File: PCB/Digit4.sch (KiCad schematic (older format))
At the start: 1 part

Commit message: Worked on PCB.
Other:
- moved on the sheet: D3D
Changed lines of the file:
@@
 L LED_Array D3
 U 4 1 54BC7685
-P 4800 4150
-F 0 "D3" H 4800 5300 50  0000 C CNN
-F 1 "LED_Array" H 4800 5400 50  0000 C CNN
-F 2 "Custom:LED-ARRAY" H 4800 5075 50  0001 C CNN
-F 3 "" H 4800 5075 50  0000 C CNN
-	4    4800 4150
+P 3750 4150
+F 0 "D3" H 3750 5300 50  0000 C CNN
+F 1 "LED_Array" H 3750 5400 50  0000 C CNN
+F 2 "Custom:LED-ARRAY" H 3750 5075 50  0001 C CNN
+F 3 "" H 3750 5075 50  0000 C CNN
+	4    3750 4150
 	1    0    0    -1
 $EndComp

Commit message: Updated schematic.
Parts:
- added Q? (x14): FDG1024NZ, SC70-6, symbol FDG1024NZ
- added R? (x14): 10K, symbol R
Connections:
- net labels added: D1A1, D1A2, D1A3, D1A4, D1A5, D1A6, D1S1G, D1S1R, D1S2G, D1S2R, D1S3G, D1S3R, D1S4G, D1S4R, D1S5G, D1S5R, D1S6G, D1S6R, D1S7G, D1S7R, GND
- wire segments 0 -> 257
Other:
- moved on the sheet: D3D

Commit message: Updated schematic.
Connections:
- net labels added: D4A1, D4A2, D4A3, D4A4, D4A5, D4A6, D4S1G, D4S1R, D4S2G, D4S2R, D4S3G, D4S3R, D4S4G, D4S4R, D4S5G, D4S5R, D4S6G, D4S6R, D4S7G, D4S7R
- net labels removed: D1A1, D1A2, D1A3, D1A4, D1A5, D1A6, D1S1G, D1S1R, D1S2G, D1S2R, D1S3G, D1S3R, D1S4G, D1S4R, D1S5G, D1S5R, D1S6G, D1S6R, D1S7G, D1S7R
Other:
- moved on the sheet: D3D, R?

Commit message: Updated mosfets.
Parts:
- removed Q? (x14): FDG1024NZ, SC70-6, symbol FDG1024NZ
- added Q? (x14): DMN2041LSD-13, SO-8, symbol DMN2041LSD-13
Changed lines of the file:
@@
 D4A6
-$Comp
-L FDG1024NZ Q?
-U 1 1 54EADD7E
-P 1350 2350
-F 0 "Q?" H 1350 2201 40  0000 R CNN
-F 1 "FDG1024NZ" H 1350 2500 40  0000 R CNN
-F 2 "SC70-6" H 1220 2452 29  0000 C CNN
-F 3 "" H 1350 2350 60  0000 C CNN
-	1    1350 2350
-	1    0    0    -1
-$EndComp
-$Comp
-L FDG1024NZ Q?
-U 1 1 54EADD85
-P 2350 2350
-F 0 "Q?" H 2350 2201 40  0000 R CNN
-F 1 "FDG1024NZ" H 2350 2500 40  0000 R CNN
-F 2 "SC70-6" H 2220 2452 29  0000 C CNN
-F 3 "" H 2350 2350 60  0000 C CNN
-	1    2350 2350
-	1    0    0    -1
-$EndComp
 $Comp
 L R R?
@@
 $EndComp
 $Comp
-L FDG1024NZ Q?
-U 1 1 54EADDA6
-P 1350 5050
-F 0 "Q?" H 1350 4901 40  0000 R CNN
-F 1 "FDG1024NZ" H 1350 5200 40  0000 R CNN
-F 2 "SC70-6" H 1220 5152 29  0000 C CNN
-F 3 "" H 1350 5050 60  0000 C CNN
-	1    1350 5050
-	1    0    0    -1
-$EndComp
-$Comp
 L R R?
 U 1 1 54EADDAD
@@
 D4S5G
 $Comp
-L FDG1024NZ Q?
-U 1 1 54EADDCB
-P 2350 5050
-F 0 "Q?" H 2350 4901 40  0000 R CNN
-F 1 "FDG1024NZ" H 2350 5200 40  0000 R CNN
-F 2 "SC70-6" H 2220 5152 29  0000 C CNN
-F 3 "" H 2350 5050 60  0000 C CNN
-	1    2350 5050
-	1    0    0    -1
-$EndComp
-$Comp
-L FDG1024NZ Q?
-U 1 1 54EADDD2
-P 1350 6825
-F 0 "Q?" H 1350 6676 40  0000 R CNN
-F 1 "FDG1024NZ" H 1350 6975 40  0000 R CNN
-F 2 "SC70-6" H 1220 6927 29  0000 C CNN
-F 3 "" H 1350 6825 60  0000 C CNN
-	1    1350 6825
-	1    0    0    -1
-$EndComp
-$Comp
 L R R?
 U 1 1 54EADDD9
@@
 Text HLabel 1900 6875 0    50   Input ~ 0
 D4S4G
-$Comp
-L FDG1024NZ Q?
-U 1 1 54EADDF5
-P 2350 6825
-F 0 "Q?" H 2350 6676 40  0000 R CNN
-F 1 "FDG1024NZ" H 2350 6975 40  0000 R CNN
-F 2 "SC70-6" H 2220 6927 29  0000 C CNN
-F 3 "" H 2350 6825 60  0000 C CNN
-	1    2350 6825
-	1    0    0    -1
-$EndComp
 Wire Wire Line
 	3705 1150 3705 950
@@
 Wire Wire Line
 	2450 6625 2450 6500
-$Comp
-L FDG1024NZ Q?
-U 1 1 54EADF15
-P 7700 1125
-F 0 "Q?" H 7700 976 40  0000 R CNN
-F 1 "FDG1024NZ" H 7700 1275 40  0000 R CNN
-F 2 "SC70-6" H 7570 1227 29  0000 C CNN
-F 3 "" H 7700 1125 60  0000 C CNN
-	1    7700 1125
-	1    0    0    -1
-$EndComp
 $Comp
 L R R?
@@
 Text HLabel 8250 1175 0    50   Input ~ 0
 D4S1G
-$Comp
-L FDG1024NZ Q?
-U 1 1 54EADF38
-P 8700 1125
-F 0 "Q?" H 8700 976 40  0000 R CNN
-F 1 "FDG1024NZ" H 8700 1275 40  0000 R CNN
-F 2 "SC70-6" H 8570 1227 29  0000 C CNN
-F 3 "" H 8700 1125 60  0000 C CNN
-	1    8700 1125
-	1    0    0    -1
-$EndComp
 Wire Wire Line
 	8250 1175 8500 1175
@@
 Wire Wire Line
 	8800 675  8800 925
-$Comp
-L FDG1024NZ Q?
-U 1 1 54EADF4E
-P 7700 2625
-F 0 "Q?" H 7700 2476 40  0000 R CNN
-F 1 "FDG1024NZ" H 7700 2775 40  0000 R CNN
-F 2 "SC70-6" H 7570 2727 29  0000 C CNN
-F 3 "" H 7700 2625 60  0000 C CNN
-	1    7700 2625
-	1    0    0    -1
-$EndComp
 $Comp
 L R R?
@@
 Text HLabel 8250 2675 0    50   Input ~ 0
 D4S2G
-$Comp
-L FDG1024NZ Q?
-U 1 1 54EADF71
-P 8700 2625
-F 0 "Q?" H 8700 2476 40  0000 R CNN
-F 1 "FDG1024NZ" H 8700 2775 40  0000 R CNN
-F 2 "SC70-6" H 8570 2727 29  0000 C CNN
-F 3 "" H 8700 2625 60  0000 C CNN
-	1    8700 2625
-	1    0    0    -1
-$EndComp
 Wire Wire Line
 	8250 2675 8500 2675
@@
 Wire Wire Line
 	8800 2125 8800 2425
-$Comp
-L FDG1024NZ Q?
-U 1 1 54EADF88
-P 7700 5485
-F 0 "Q?" H 7700 5336 40  0000 R CNN
-F 1 "FDG1024NZ" H 7700 5635 40  0000 R CNN
-F 2 "SC70-6" H 7570 5587 29  0000 C CNN
-F 3 "" H 7700 5485 60  0000 C CNN
-	1    7700 5485
-	1    0    0    -1
-$EndComp
 $Comp
 L R R?
@@
 Text HLabel 8250 5535 0    50   Input ~ 0
 D4S3G
-$Comp
-L FDG1024NZ Q?
-U 1 1 54EADFAB
-P 8700 5485
-F 0 "Q?" H 8700 5336 40  0000 R CNN
-F 1 "FDG1024NZ" H 8700 5635 40  0000 R CNN
-F 2 "SC70-6" H 8570 5587 29  0000 C CNN
-F 3 "" H 8700 5485 60  0000 C CNN
-	1    8700 5485
-	1    0    0    -1
-$EndComp
 Wire Wire Line
 	8250 5535 8500 5535
@@
 Wire Wire Line
 	7800 750  7800 925
-$Comp
-L FDG1024NZ Q?
-U 1 1 54EADFC3
-P 7700 4010
-F 0 "Q?" H 7700 3861 40  0000 R CNN
-F 1 "FDG1024NZ" H 7700 4160 40  0000 R CNN
-F 2 "SC70-6" H 7570 4112 29  0000 C CNN
-F 3 "" H 7700 4010 60  0000 C CNN
-	1    7700 4010
-	1    0    0    -1
-$EndComp
 $Comp
 L R R?
@@
 Text HLabel 8250 4060 0    50   Input ~ 0
 D4S7G
-$Comp
-L FDG1024NZ Q?
-U 1 1 54EADFE6
-P 8700 4010
-F 0 "Q?" H 8700 3861 40  0000 R CNN
-F 1 "FDG1024NZ" H 8700 4160 40  0000 R CNN
-F 2 "SC70-6" H 8570 4112 29  0000 C CNN
-F 3 "" H 8700 4010 60  0000 C CNN
-	1    8700 4010
-	1    0    0    -1
-$EndComp
 Wire Wire Line
 	8250 4060 8500 4060
@@
 EndData
 $EndBitmap
+$Comp
+L DMN2041LSD-13 Q?
+U 1 1 54ED5347
+P 1350 2350
+F 0 "Q?" H 1350 2201 40  0000 R CNN
+F 1 "DMN2041LSD-13" H 1350 2500 40  0000 R CNN
+F 2 "SO-8" H 1220 2452 29  0001 C CNN
+F 3 "" H 1350 2350 60  0000 C CNN
+	1    1350 2350
+	1    0    0    -1
+$EndComp
+$Comp
+L DMN2041LSD-13 Q?
+U 2 1 54ED5384
+P 2350 2350
+F 0 "Q?" H 2350 2201 40  0000 R CNN
+F 1 "DMN2041LSD-13" H 2350 2500 40  0000 R CNN
+F 2 "SO-8" H 2220 2452 29  0001 C CNN
+F 3 "" H 2350 2350 60  0000 C CNN
+	2    2350 2350
+	1    0    0    -1
+$EndComp
+$Comp
+L DMN2041LSD-13 Q?
+U 1 1 54ED5743
+P 1350 5050
+F 0 "Q?" H 1350 4901 40  0000 R CNN
+F 1 "DMN2041LSD-13" H 1350 5200 40  0000 R CNN
+F 2 "SO-8" H 1220 5152 29  0001 C CNN
+F 3 "" H 1350 5050 60  0000 C CNN
+	1    1350 5050
+	1    0    0    -1
+$EndComp
+$Comp
+L DMN2041LSD-13 Q?
+U 2 1 54ED577C
+P 2350 5050
+F 0 "Q?" H 2350 4901 40  0000 R CNN
+F 1 "DMN2041LSD-13" H 2350 5200 40  0000 R CNN
+F 2 "SO-8" H 2220 5152 29  0001 C CNN
+F 3 "" H 2350 5050 60  0000 C CNN
+	2    2350 5050
+	1    0    0    -1
+$EndComp
+$Comp
+L DMN2041LSD-13 Q?
+U 1 1 54ED5997
+P 1350 6825
+F 0 "Q?" H 1350 6676 40  0000 R CNN
+F 1 "DMN2041LSD-13" H 1350 6975 40  0000 R CNN
+F 2 "SO-8" H 1220 6927 29  0001 C CNN
+F 3 "" H 1350 6825 60  0000 C CNN
+	1    1350 6825
+	1    0    0    -1
+$EndComp
+$Comp
+L DMN2041LSD-13 Q?
+U 2 1 54ED5AEE
+P 2350 6825
+F 0 "Q?" H 2350 6676 40  0000 R CNN
+F 1 "DMN2041LSD-13" H 2350 6975 40  0000 R CNN
+F 2 "SO-8" H 2220 6927 29  0001 C CNN
+F 3 "" H 2350 6825 60  0000 C CNN
+	2    2350 6825
+	1    0    0    -1
+$EndComp
+$Comp
+L DMN2041LSD-13 Q?
+U 1 1 54ED5CA8
+P 7700 5485
+F 0 "Q?" H 7700 5336 40  0000 R CNN
+F 1 "DMN2041LSD-13" H 7700 5635 40  0000 R CNN
+F 2 "SO-8" H 7570 5587 29  0001 C CNN
+F 3 "" H 7700 5485 60  0000 C CNN
+	1    7700 5485
+	1    0    0    -1
+$EndComp
+$Comp
+L DMN2041LSD-13 Q?
+U 2 1 54ED5D85
+P 8700 5485
+F 0 "Q?" H 8700 5336 40  0000 R CNN
+F 1 "DMN2041LSD-13" H 8700 5635 40  0000 R CNN
+F 2 "SO-8" H 8570 5587 29  0001 C CNN
+F 3 "" H 8700 5485 60  0000 C CNN
+	2    8700 5485
+	1    0    0    -1
+$EndComp
+$Comp
+L DMN2041LSD-13 Q?
+U 1 1 54ED5ECB
+P 7700 4010
+F 0 "Q?" H 7700 3861 40  0000 R CNN
+F 1 "DMN2041LSD-13" H 7700 4160 40  0000 R CNN
+F 2 "SO-8" H 7570 4112 29  0001 C CNN
+F 3 "" H 7700 4010 60  0000 C CNN
+	1    7700 4010
+	1    0    0    -1
+$EndComp
+$Comp
+L DMN2041LSD-13 Q?
+U 2 1 54ED5F20
+P 8700 4010
+F 0 "Q?" H 8700 3861 40  0000 R CNN
+F 1 "DMN2041LSD-13" H 8700 4160 40  0000 R CNN
+F 2 "SO-8" H 8570 4112 29  0001 C CNN
+F 3 "" H 8700 4010 60  0000 C CNN
+	2    8700 4010
+	1    0    0    -1
+$EndComp
+$Comp
+L DMN2041LSD-13 Q?
+U 1 1 54ED6335
+P 7700 2625
+F 0 "Q?" H 7700 2476 40  0000 R CNN
+F 1 "DMN2041LSD-13" H 7700 2775 40  0000 R CNN
+F 2 "SO-8" H 7570 2727 29  0001 C CNN
+F 3 "" H 7700 2625 60  0000 C CNN
+	1    7700 2625
+	1    0    0    -1
+$EndComp
+$Comp
+L DMN2041LSD-13 Q?
+U 2 1 54ED63B0
+P 8700 2625
+F 0 "Q?" H 8700 2476 40  0000 R CNN
+F 1 "DMN2041LSD-13" H 8700 2775 40  0000 R CNN
+F 2 "SO-8" H 8570 2727 29  0001 C CNN
+F 3 "" H 8700 2625 60  0000 C CNN
+	2    8700 2625
+	1    0    0    -1
+$EndComp
+$Comp
+L DMN2041LSD-13 Q?
+U 1 1 54ED6543
+P 7700 1125
+F 0 "Q?" H 7700 976 40  0000 R CNN
+F 1 "DMN2041LSD-13" H 7700 1275 40  0000 R CNN
+F 2 "SO-8" H 7570 1227 29  0001 C CNN
+F 3 "" H 7700 1125 60  0000 C CNN
+	1    7700 1125
+	1    0    0    -1
+$EndComp
+$Comp
+L DMN2041LSD-13 Q?
+U 2 1 54ED65B8
+P 8700 1125
+F 0 "Q?" H 8700 976 40  0000 R CNN
+F 1 "DMN2041LSD-13" H 8700 1275 40  0000 R CNN
+F 2 "SO-8" H 8570 1227 29  0001 C CNN
+F 3 "" H 8700 1125 60  0000 C CNN
+	2    8700 1125
+	1    0    0    -1
+$EndComp
 $EndSCHEMATC

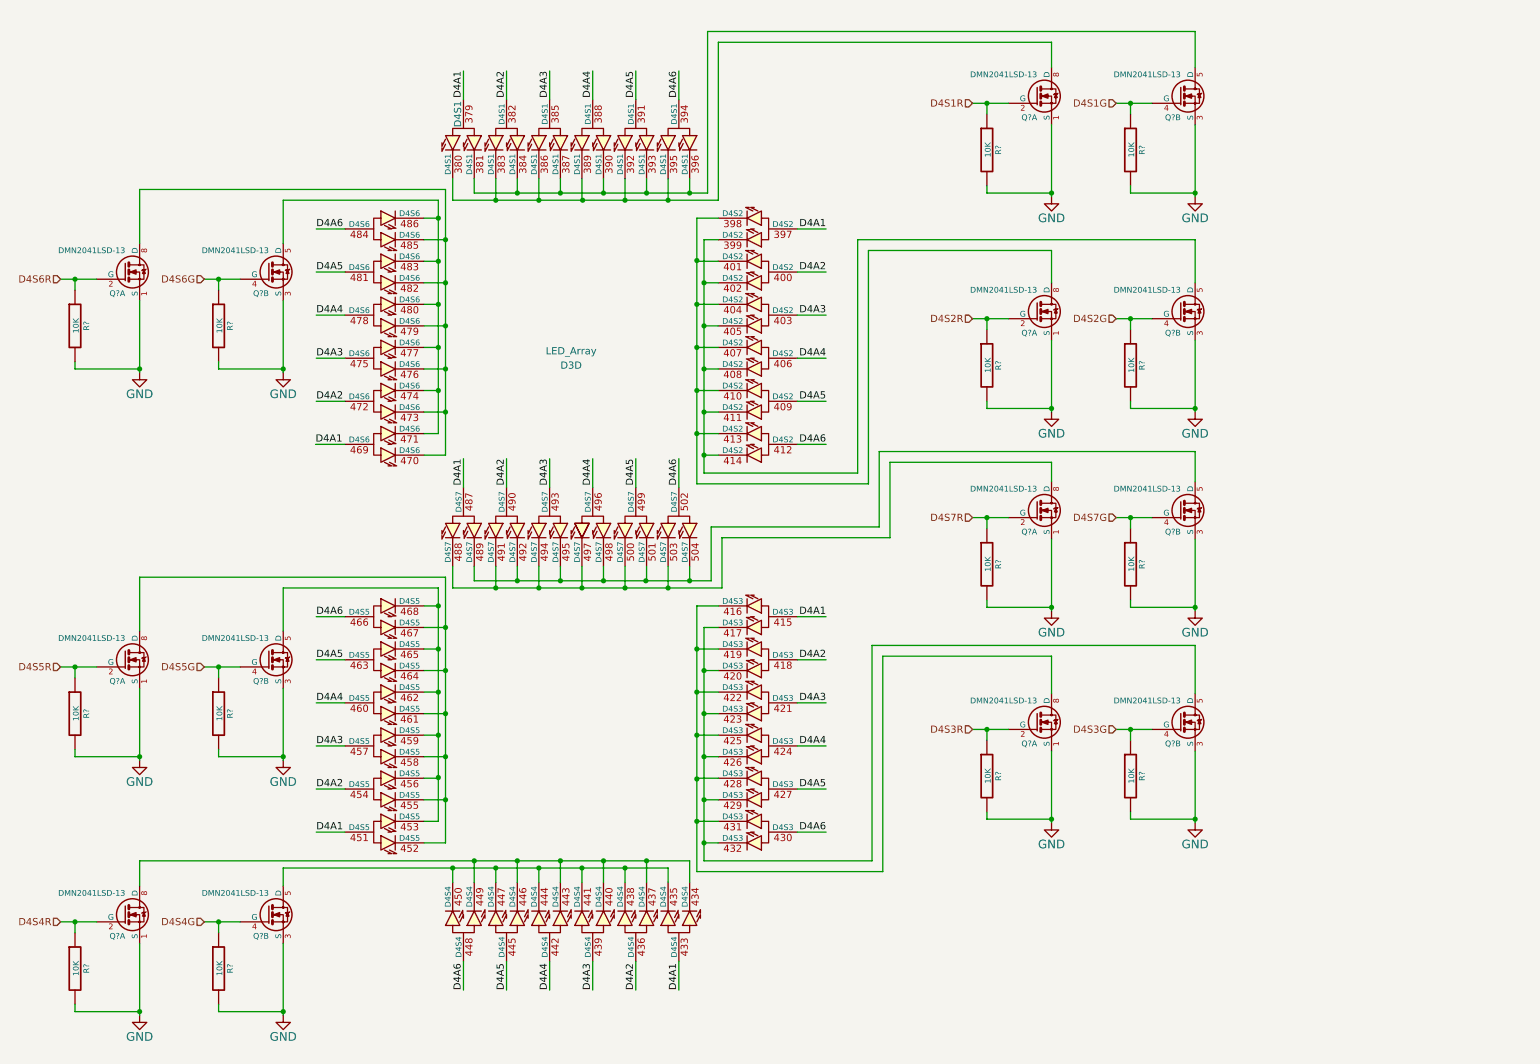
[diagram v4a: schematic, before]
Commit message: Added additional mosfets.
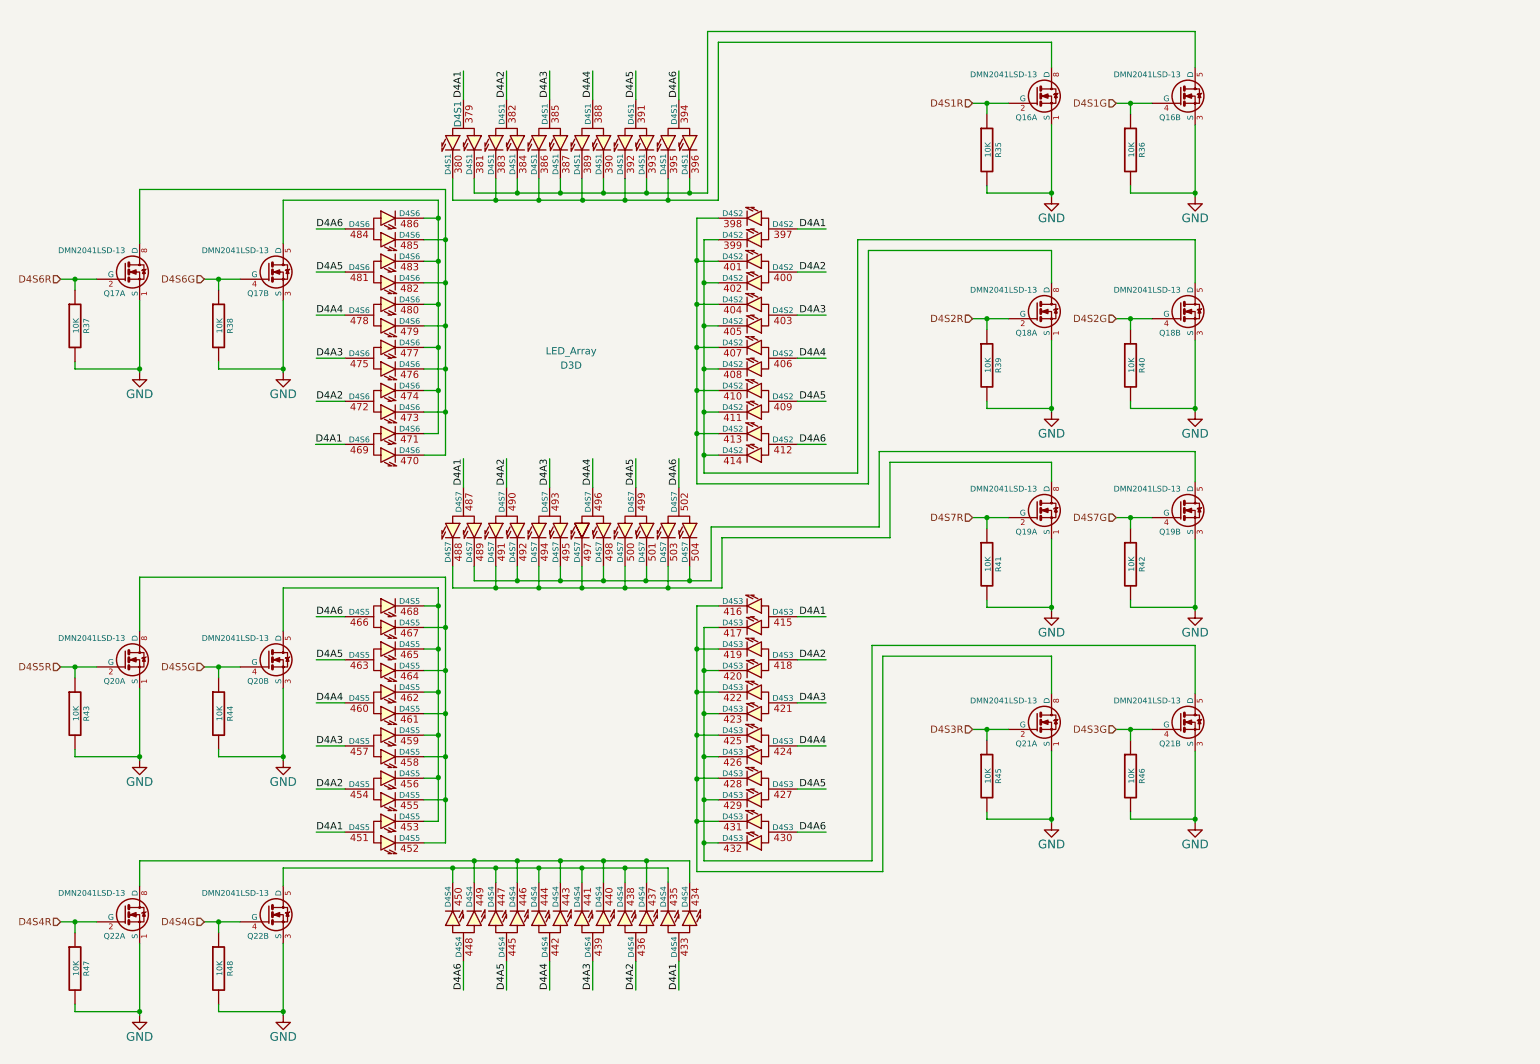
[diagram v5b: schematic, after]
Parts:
- Q16, Q17, Q18, Q19, Q20, Q21, Q22: renamed from Q?; footprint SO-8 -> Power_Integrations:SO-8
- R35, R36, R37, R38, R39, R40, R41, R42, R43, R44, R45, R46, R47, R48: renamed from R?; footprint (none) -> Resistors_SMD:R_0603_HandSoldering

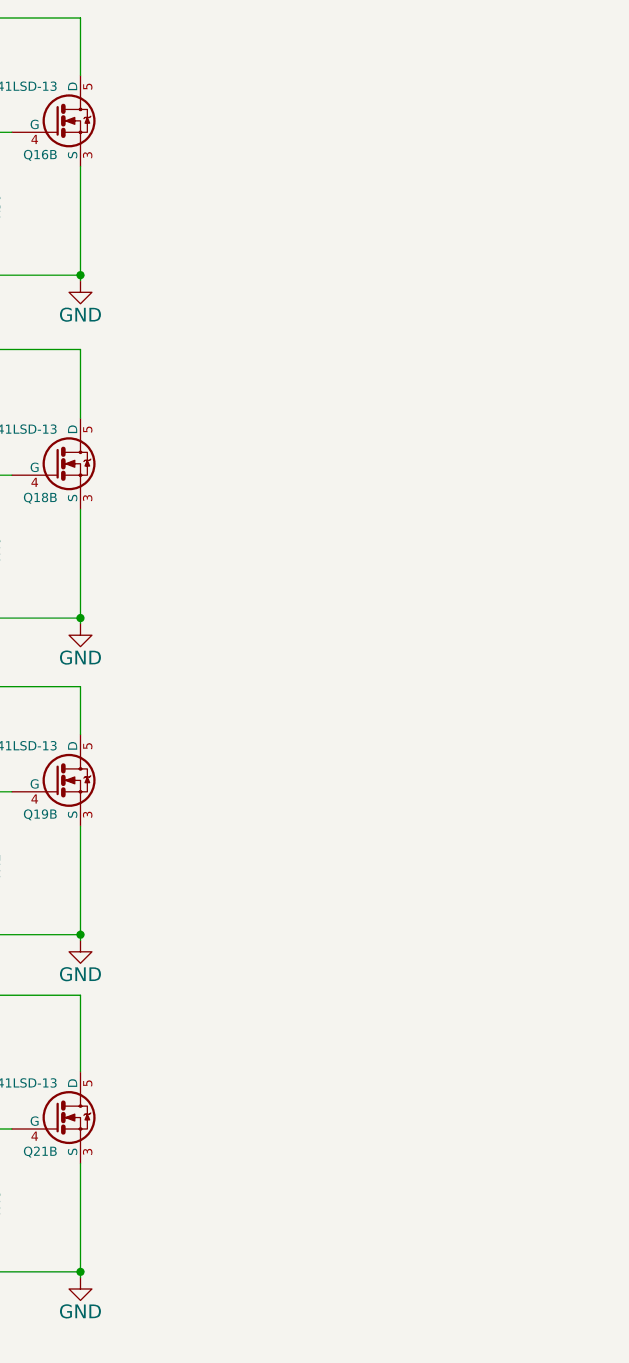
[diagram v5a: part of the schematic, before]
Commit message: Added additional mosfets.
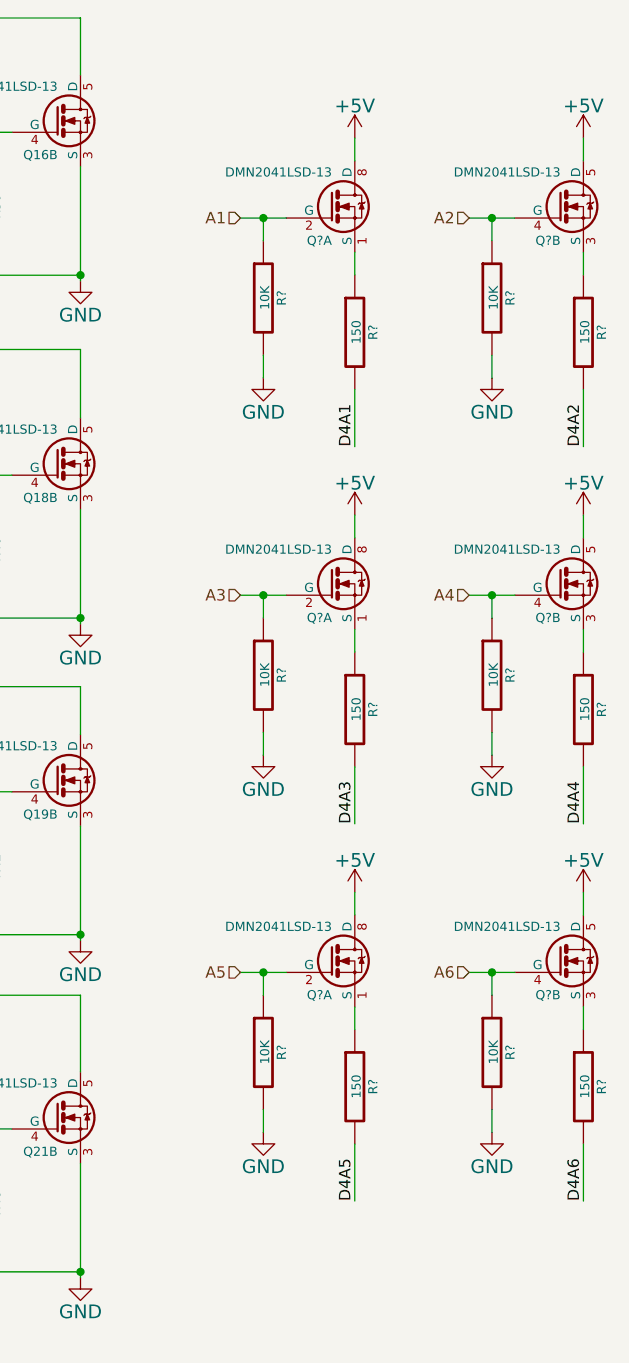
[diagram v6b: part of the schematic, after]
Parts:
- added Q? (x6): DMN2041LSD-13, SO-8, symbol DMN2041LSD-13
- added R? (x6): 10K, Resistors_SMD:R_0603_HandSoldering, symbol R
- added R? (x6): 150, Resistors_SMD:R_0603_HandSoldering, symbol R
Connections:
- net D4A1: now also R?.2
- net D4A2: now also R?.2
- net D4A3: now also R?.2
- net D4A4: now also R?.2
- net D4A5: now also R?.2
- net D4A6: now also R?.2
- net GND: now also R?.2, R?.2, R?.2, R?.2, R?.2, R?.2
- new net: Q?.1 (S), R?.1 (x3)
- new net: Q?.3 (S), R?.1 (x3)
- new net +5V: Q?.5 (D), Q?.5 (D), Q?.5 (D), Q?.8 (D), Q?.8 (D), Q?.8 (D)
- new net A1: Q?.2 (G), R?.1
- new net A2: Q?.4 (G), R?.1
- new net A3: Q?.2 (G), R?.1
- new net A4: Q?.4 (G), R?.1
- new net A5: Q?.2 (G), R?.1
- new net A6: Q?.4 (G), R?.1

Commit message: Edit PCB.
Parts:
- gave numbers to parts that had none: 15

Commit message: PCB work.
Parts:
- removed Q30, Q31, Q32: DMN2041LSD-13, SO-8, symbol DMN2041LSD-13
- removed R63, R64, R67, R68, R71, R72: 10K, Resistors_SMD:R_0603_HandSoldering, symbol R
- removed R65, R66, R69, R70, R73, R74: 150, Resistors_SMD:R_0603_HandSoldering, symbol R
- renumbered Q21 to Q10, Q22 to Q11, Q16 to Q5, Q17 to Q6, Q18 to Q7, Q19 to Q8, Q20 to Q9, R35 to R19, R36 to R20, R37 to R21, R38 to R22, R39 to R23, R40 to R24, R41 to R25, R42 to R26, R43 to R27, R44 to R28, R45 to R29, R46 to R30, R47 to R31, R48 to R32
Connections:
- net D4A1 is gone; now on net A1: D3.379 (D4S1), D3.397 (D4S2), D3.415 (D4S3), D3.433 (D4S4), D3.451 (D4S5), D3.469 (D4S6), D3.487 (D4S7)
- net D4A2 is gone; now on net A2: D3.382 (D4S1), D3.400 (D4S2), D3.418 (D4S3), D3.436 (D4S4), D3.454 (D4S5), D3.472 (D4S6), D3.490 (D4S7)
- net D4A3 is gone; now on net A3: D3.385 (D4S1), D3.403 (D4S2), D3.421 (D4S3), D3.439 (D4S4), D3.457 (D4S5), D3.475 (D4S6), D3.493 (D4S7)
- net D4A4 is gone; now on net A4: D3.388 (D4S1), D3.406 (D4S2), D3.424 (D4S3), D3.442 (D4S4), D3.460 (D4S5), D3.478 (D4S6), D3.496 (D4S7)
- net D4A5 is gone; now on net A5: D3.391 (D4S1), D3.409 (D4S2), D3.427 (D4S3), D3.445 (D4S4), D3.463 (D4S5), D3.481 (D4S6), D3.499 (D4S7)
- net D4A6 is gone; now on net A6: D3.394 (D4S1), D3.412 (D4S2), D3.430 (D4S3), D3.448 (D4S4), D3.466 (D4S5), D3.484 (D4S6), D3.502 (D4S7)
